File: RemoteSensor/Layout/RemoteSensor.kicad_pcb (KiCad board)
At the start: 2 copper layers, 50.8 x 50.8 mm, 47 parts, among them J1 PRG_HEADER, J2 LCD_HEADER, J3 USB_B_Micro, J4 Conn_01x02_Male, Q1 2N7002, Q2 2N7002, Q3 2N7002, SW1 BTN_RST, SW2 BTN_LOAD, SW3 SW_DPDT_x2, U1 ESP-12F, U2 74LVC2G02, U3 LM50CIM3, U4 MCP73831-2-OT, U5 LM3670MF, U6 BD48ExxG, U7 BD48ExxG

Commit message: Finalize PCB
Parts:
- J3: footprint Connector_USB:USB_Micro-B_Molex-105133-0031 -> Connector_USB:USB_Micro-B_Molex_47346-0001
- J4: value Conn_01x02_Male -> BATT_CONN; moved to B.Cu
- Q1, Q2, Q3, R1, R14, R15, R2, R3, R4, R5, R6, U2, U6, U7: moved to B.Cu
- moved D1 117.2 mm to (186.7, 138.6)
- moved S1 114.5 mm to (198.1, 115.4), turned to 270 degrees
- moved U1 113.9 mm to (180.8, 118.0), turned to 180 degrees
- moved U2 102.9 mm to (180.9, 116.3), turned to 180 degrees
- moved Q1 101.0 mm to (194.3, 115.3), turned to 180 degrees
- moved J3 98.8 mm to (175.4, 93.9), turned to 180 degrees
- moved R1 97.5 mm to (184.4, 119.2), turned to 90 degrees
- moved Q2 94.6 mm to (176.0, 137.3)
- moved U3 94.1 mm to (176.0, 137.4), turned to 180 degrees
- moved R8 92.9 mm to (186.7, 136.3)
- moved D2 86.1 mm to (166.7, 138.6)
- moved U6 84.7 mm to (164.3, 127.7), turned to 180 degrees
- moved R4 84.6 mm to (184.4, 114.9), turned to 90 degrees
- moved SW2 84.3 mm to (164.3, 127.7)
- moved C5 84.0 mm to (191.3, 101.8), turned to 90 degrees
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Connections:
- J3 pad 6: Net-(J3-Pad6) -> GND
- J4 pad 1: (no net) -> GND
- J4 pad 2: (no net) -> V_BATT
- R3 pad 1: /WAKE_PIN -> /HB_PIN
- U1 pad 16: (no net) -> /SLEEP_PIN
- U2 pad 6: /WAKE_PIN -> /HB_PIN
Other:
- outline, holes or cut-outs redrawn

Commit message: Autotrace
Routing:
- net GND: track 0.00 -> 335.7 mm
- net 3.3V: track 0.00 -> 149.5 mm, vias 0 -> 1
- net /RST: track 0.00 -> 67.6 mm, vias 0 -> 2
- net /WAKE_STS: track 0.00 -> 59.2 mm, vias 0 -> 1
- net /HB_PIN: track 0.00 -> 55.6 mm, vias 0 -> 1
- net /SCL: track 0.00 -> 50.2 mm, vias 0 -> 1
- net /UP_PIN: track 0.00 -> 40.5 mm
- net /BATT_STS: track 0.00 -> 38.7 mm, vias 0 -> 1
- net V_BATT: track 0.00 -> 38.1 mm, vias 0 -> 1
- net /SDA: track 0.00 -> 38.1 mm, vias 0 -> 2
- net /CHARGE_STS: track 0.00 -> 37.4 mm
- net /RADIO_TX: track 0.00 -> 27.9 mm, vias 0 -> 2
- net /TEMP_PIN: track 0.00 -> 27.3 mm
- net /CHARGER_STS: track 0.00 -> 26.0 mm, vias 0 -> 1
- net /BATT_PIN: track 0.00 -> 24.1 mm
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
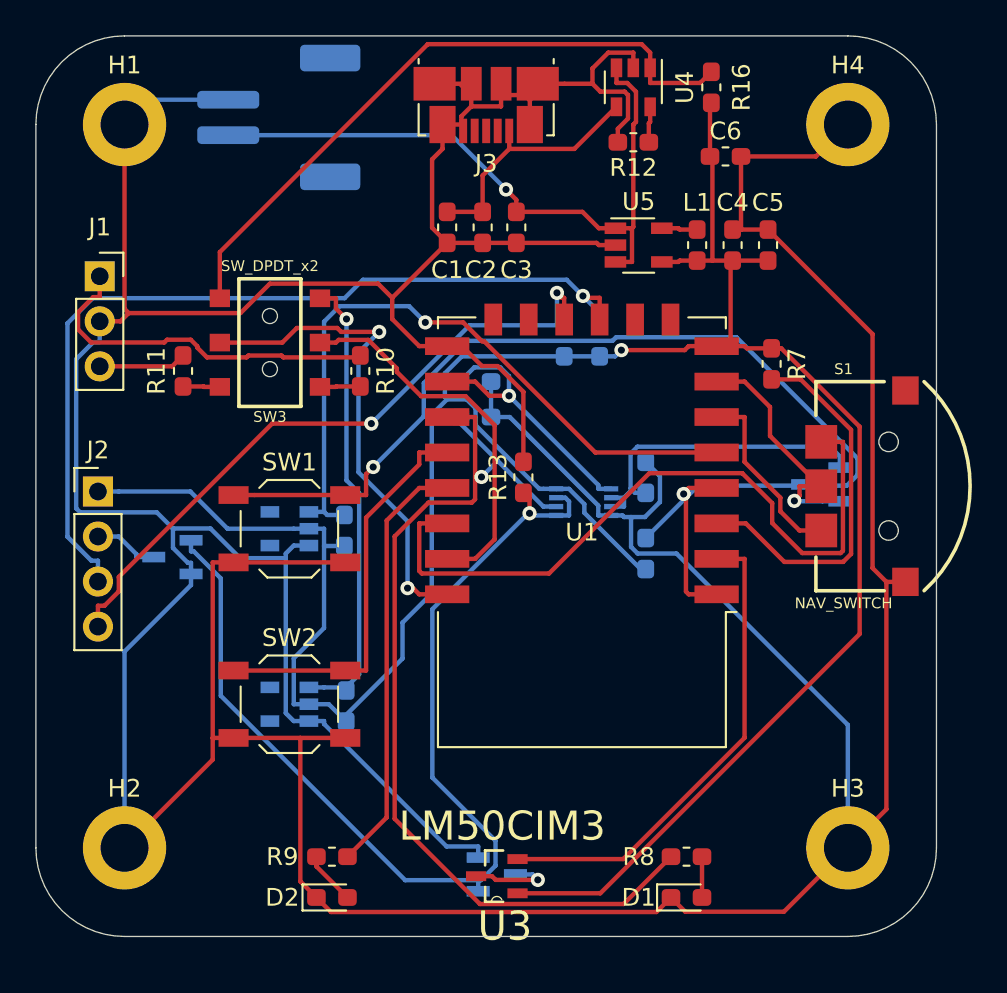
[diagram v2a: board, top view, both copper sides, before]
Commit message: Copper pour
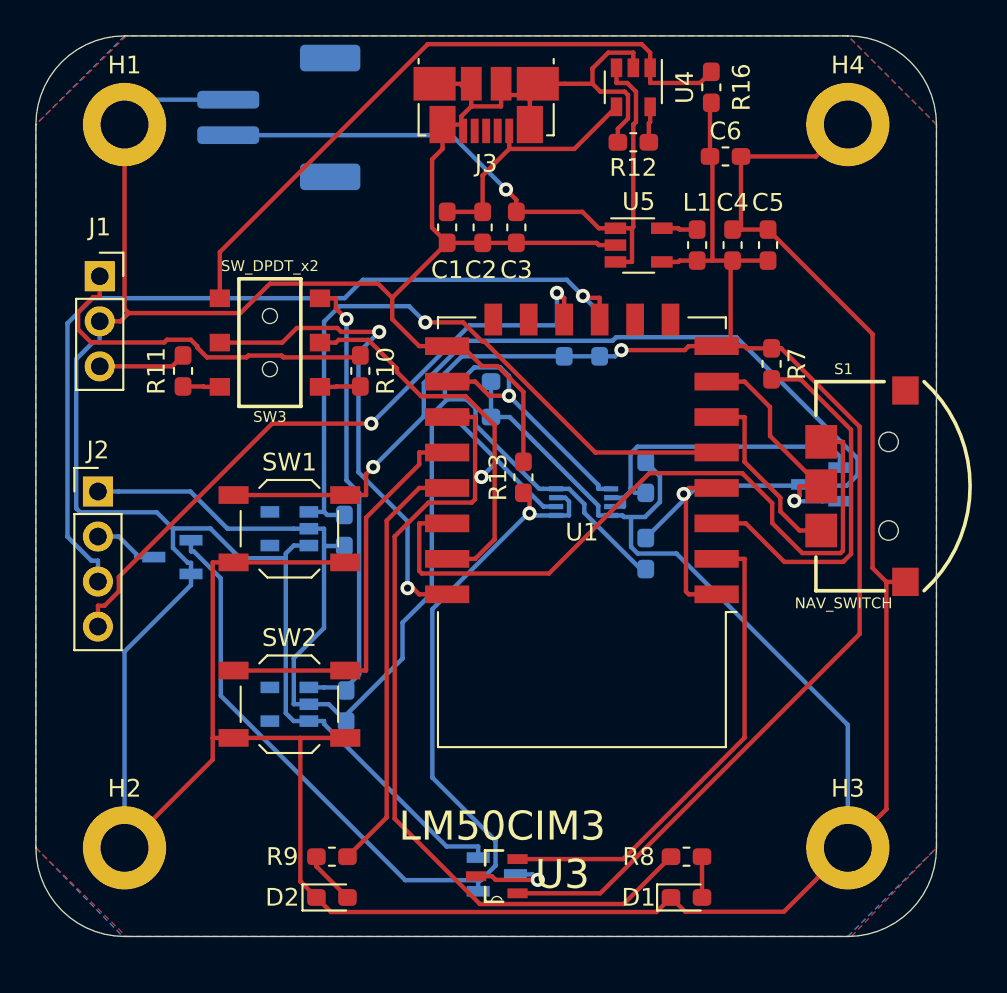
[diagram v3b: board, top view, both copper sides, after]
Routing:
- added copper zone on B.Cu, net GND
- added copper zone on F.Cu, net GND
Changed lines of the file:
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@@
     (at 176 137.4 180)
     (attr smd)
-    (fp_text reference U3 (at -0.45775 -2.82278) (layer F.SilkS)
+    (fp_text reference U3 (at -3.7 0.1) (layer F.SilkS)
       (effects (font (size 1.64196 1.64196) (thickness 0.05)))
     )
@@
       )
     )
+  )
+  (zone (net 1) (net_name GND) (layer F.Cu) (hatch edge 0.508)
+    (connect_pads (clearance 0.508))
+    (min_thickness 0.254)
+    (fill yes (arc_segments 32) (thermal_gap 0.508) (thermal_bridge_width 0.508))
+    (polygon
+      (pts
+        (xy 155.1 90) (xy 150 95) (xy 150 135.8) (xy 155.1 140.8) (xy 196 140.8)
+        (xy 200.8 135.8) (xy 200.8 95) (xy 195.8 90)
+      )
+    )
+  )
+  (zone (net 1) (net_name GND) (layer B.Cu) (hatch edge 0.508)
+    (connect_pads (clearance 0.508))
+    (min_thickness 0.254)
+    (fill yes (arc_segments 32) (thermal_gap 0.508) (thermal_bridge_width 0.508))
+    (polygon
+      (pts
+        (xy 155 90) (xy 150 95) (xy 150 135.8) (xy 154.9 140.8) (xy 195.8 140.8)
+        (xy 200.8 135.8) (xy 200.8 95) (xy 195.8 90)
+      )
+    )

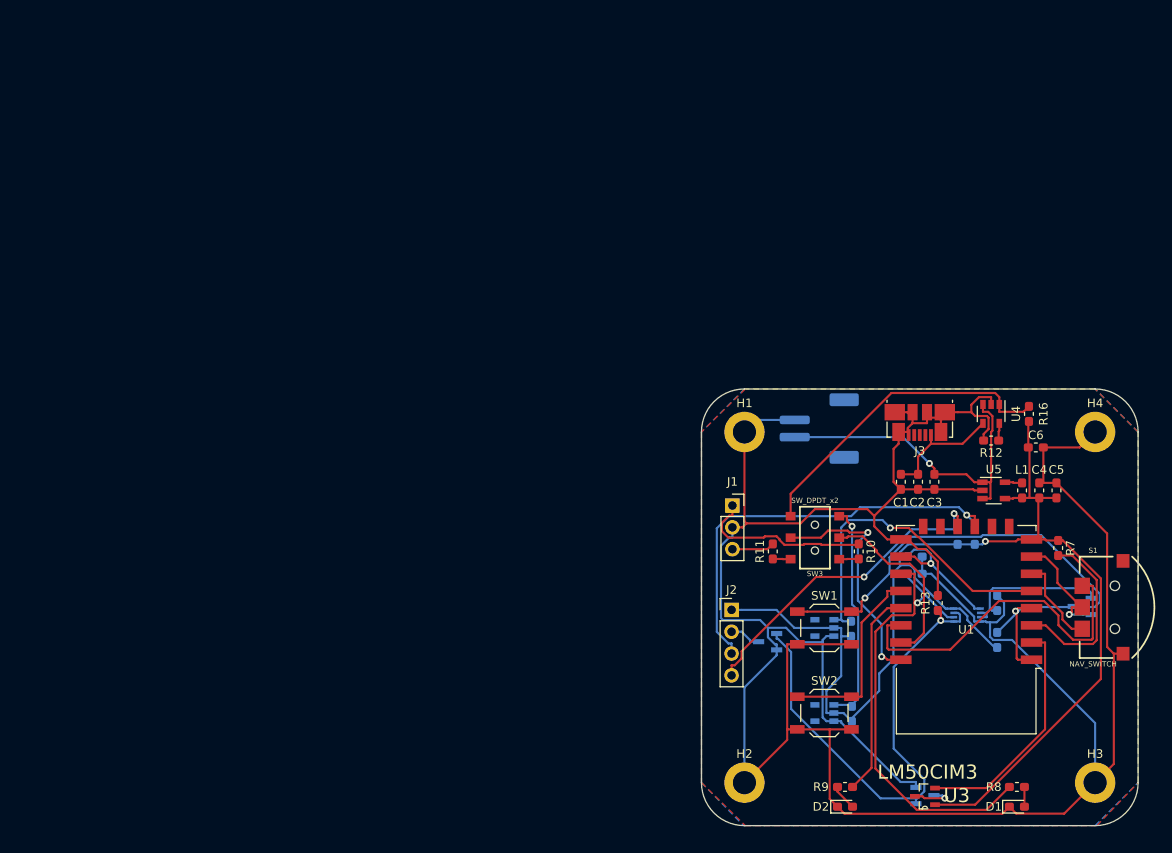
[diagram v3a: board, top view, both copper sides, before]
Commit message: Fix resistor on wrong side
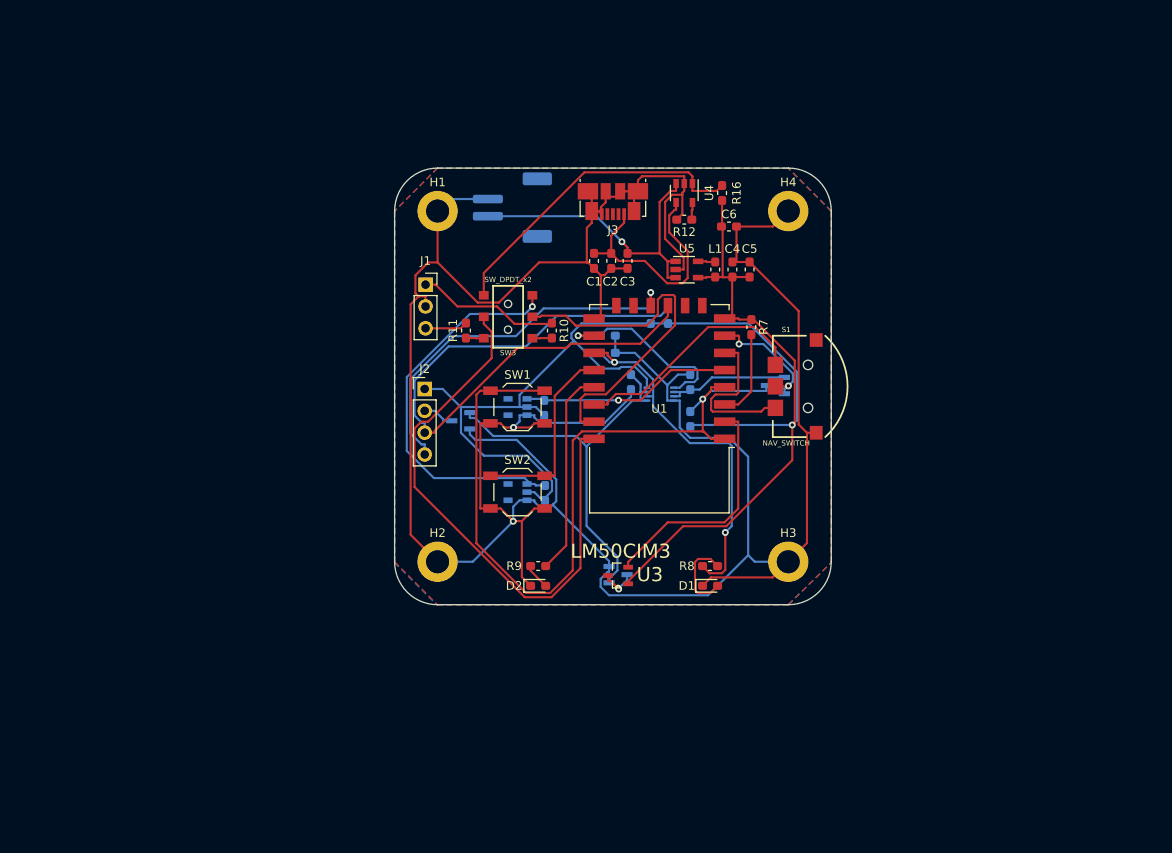
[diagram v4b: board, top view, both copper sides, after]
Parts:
- R13: moved to B.Cu
- moved H3 44.0 mm to (160.1, 110.1)
- moved C4 44.0 mm to (153.6, 76.1)
- moved C5 44.0 mm to (155.6, 76.1)
- moved C6 44.0 mm to (153.2, 71.1)
- moved H2 44.0 mm to (119.3, 110.1)
- moved H4 44.0 mm to (160.1, 69.3)
- moved J3 44.0 mm to (139.7, 68.2)
- moved L1 44.0 mm to (151.6, 76.1)
- moved Q1 44.0 mm to (158.6, 89.6)
- moved R1 44.0 mm to (148.7, 93.5)
- moved R10 44.0 mm to (132.6, 83.2)
- moved R11 44.0 mm to (122.6, 83.2)
- moved R15 44.0 mm to (131.7, 92.2)
- moved R2 44.0 mm to (139.1, 83.8)
- moved R3 44.0 mm to (139.1, 85.8)
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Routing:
- net /RADIO_TX: track 27.9 -> 67.0 mm, vias 2 -> 0
- net /SCL: track 50.2 -> 75.0 mm, vias 1 -> 0
- net 3.3V: track 149.5 -> 173.2 mm
- net /RST: track 67.6 -> 91.3 mm, vias 2 -> 1
- net GND: track 335.7 -> 356.0 mm, vias 0 -> 2
- net /RADIO_RX: track 21.6 -> 41.8 mm
- net /CHARGER_STS: track 26.0 -> 46.1 mm
- net /BATT_STS: track 38.7 -> 24.5 mm
- net V_USB: track 14.2 -> 27.9 mm
- net /UP_PIN: track 40.5 -> 28.0 mm
- net /HB_PIN: track 55.6 -> 43.2 mm, vias 1 -> 2
- net /WAKE_STS: track 59.2 -> 46.9 mm, vias 1 -> 0
- net Net-(R7-Pad2): track 21.3 -> 10.3 mm
- net /DOWN_PIN: track 10.5 -> 18.7 mm
- net Net-(D1-Pad2): track 2.30 -> 9.49 mm
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
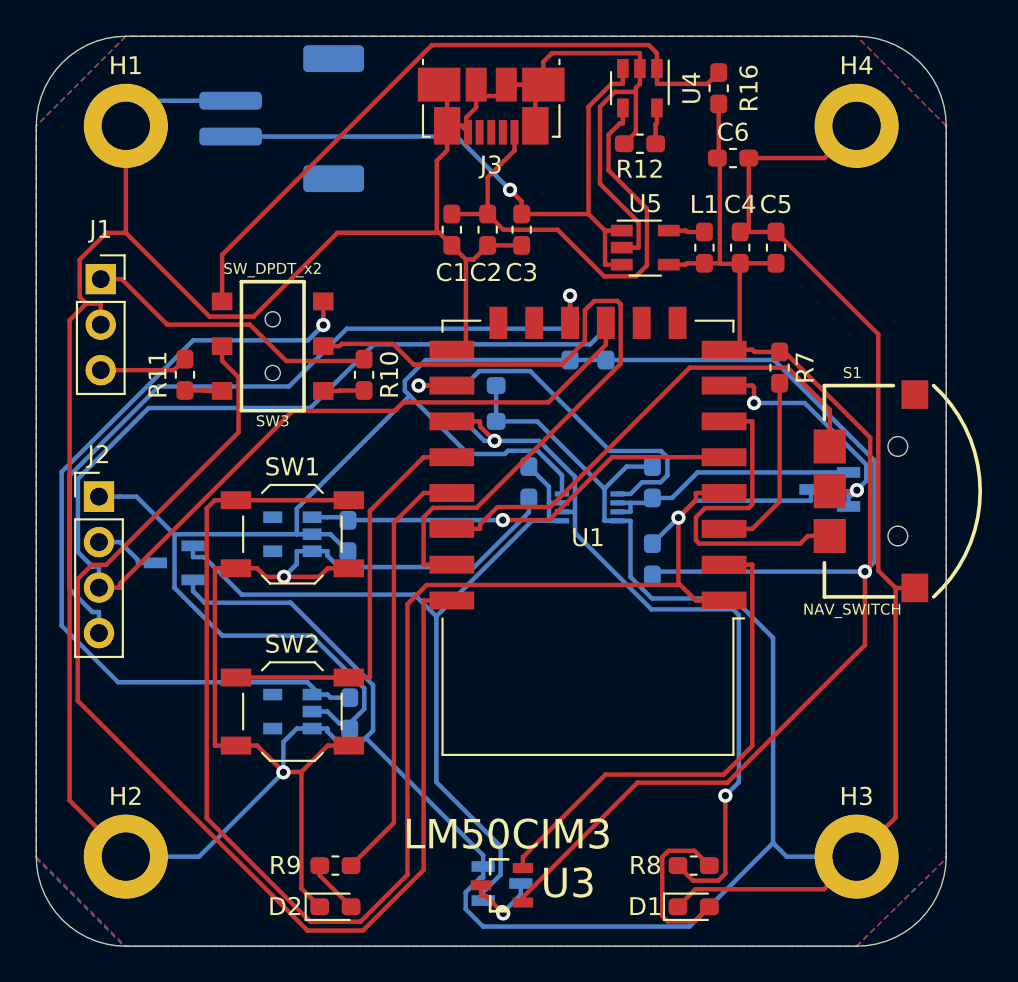
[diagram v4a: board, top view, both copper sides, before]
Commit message: Fix charger and battery status
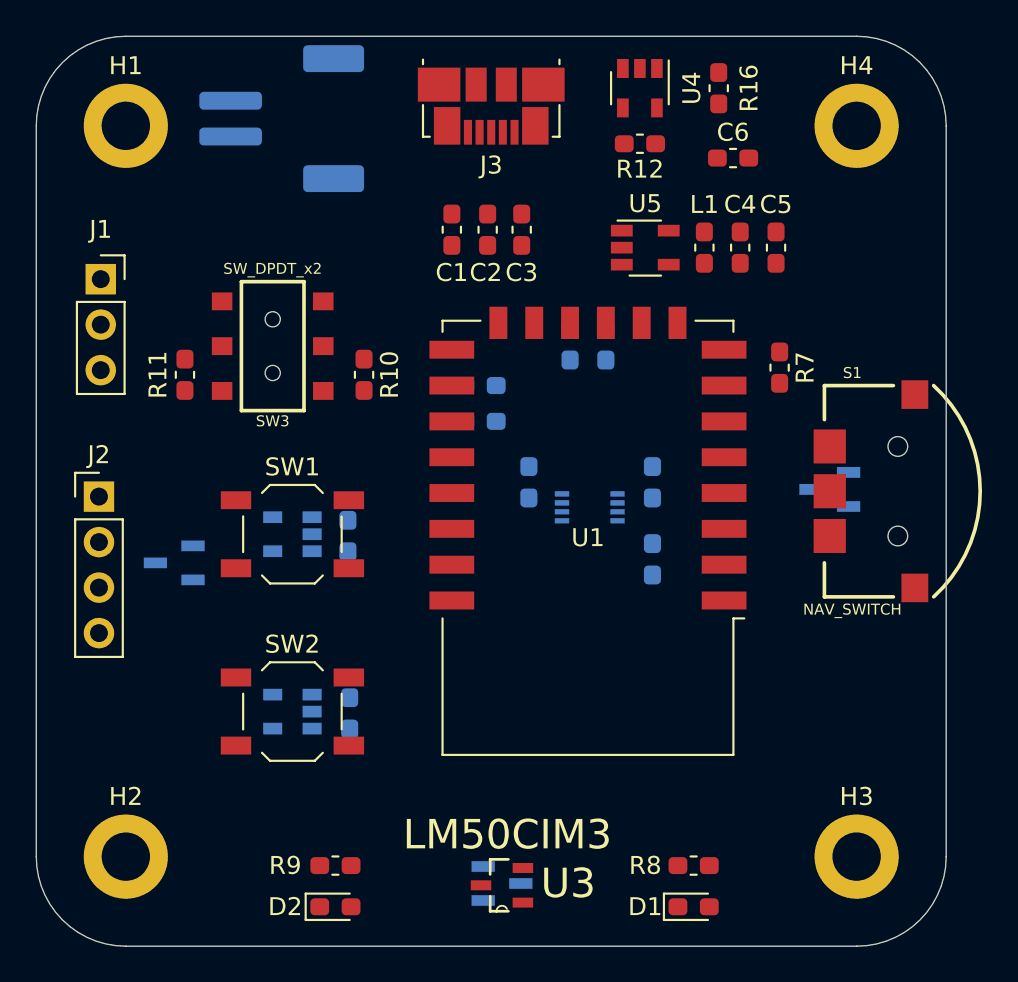
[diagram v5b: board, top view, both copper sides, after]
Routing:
- net GND: track 356.0 -> 0.00 mm, vias 2 -> 0
- net 3.3V: track 173.2 -> 0.00 mm, vias 1 -> 0
- net /RST: track 91.3 -> 0.00 mm, vias 1 -> 0
- net /SCL: track 75.0 -> 0.00 mm
- net /RADIO_TX: track 67.0 -> 0.00 mm
- net /WAKE_STS: track 46.9 -> 0.00 mm
- net /CHARGER_STS: track 46.1 -> 0.00 mm, vias 1 -> 0
- net /SDA: track 44.4 -> 0.00 mm, vias 1 -> 0
- net /HB_PIN: track 43.2 -> 0.00 mm, vias 2 -> 0
- net /RADIO_RX: track 41.8 -> 0.00 mm
- net /CHARGE_STS: track 37.3 -> 0.00 mm
- net V_BATT: track 36.6 -> 0.00 mm, vias 1 -> 0
- net /UP_PIN: track 28.0 -> 0.00 mm
- net V_USB: track 27.9 -> 0.00 mm
- net /TEMP_PIN: track 27.7 -> 0.00 mm
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- removed copper zone on B.Cu, net GND
- removed copper zone on F.Cu, net GND
